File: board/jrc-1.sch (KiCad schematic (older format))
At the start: 0 parts

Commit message: WIP
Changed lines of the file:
@@
 $Descr USLetter 11000 8500
 encoding utf-8
-Sheet 1 2
+Sheet 1 8
 Title "JRC-3"
 Date ""
@@
 $EndDescr
 $Sheet
-S 2600 2450 2350 1550
+S 900  900  1150 750
 U 60EE1618
 F0 "Sheet60EE1617" 50
-F1 "core.sch" 50
+F1 "cpu.sch" 50
+$EndSheet
+$Sheet
+S 3400 900  1150 750
+U 61B43476
+F0 "VIA" 50
+F1 "via.sch" 50
+$EndSheet
+$Sheet
+S 4650 900  1150 750
+U 62053498
+F0 "UART" 50
+F1 "uart.sch" 50
+$EndSheet
+$Sheet
+S 2150 1900 1150 750
+U 61ADDFAC
+F0 "Sheet61ADDFAB" 50
+F1 "memory.sch" 50
+$EndSheet
+$Sheet
+S 5900 850  1150 750
+U 626CE278
+F0 "Clock Circuit" 50
+F1 "clock.sch" 50
+$EndSheet
+$Sheet
+S 3900 1900 1700 1250
+U 62BE9D15
+F0 "Ports & Slots" 50
+F1 "ports.sch" 50
+$EndSheet
+$Sheet
+S 2150 900  1150 750
+U 6224E7FB
+F0 "CPLD Logic" 50
+F1 "cpld.sch" 50
 $EndSheet
 $EndSCHEMATC

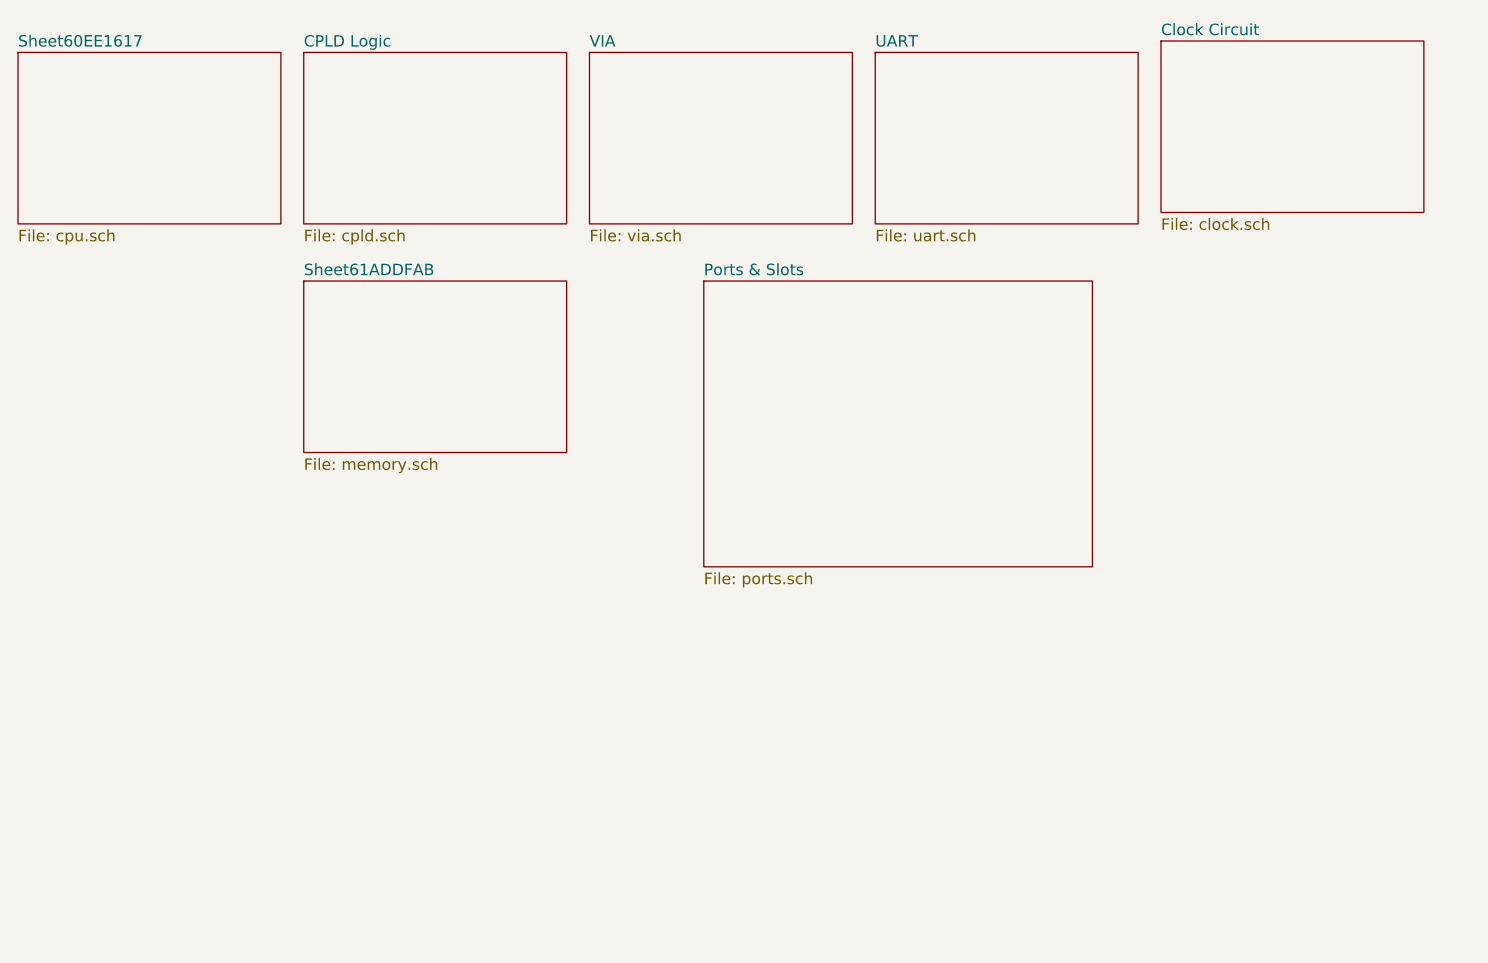
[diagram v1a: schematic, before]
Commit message: RC1 of schematic and initial board layout
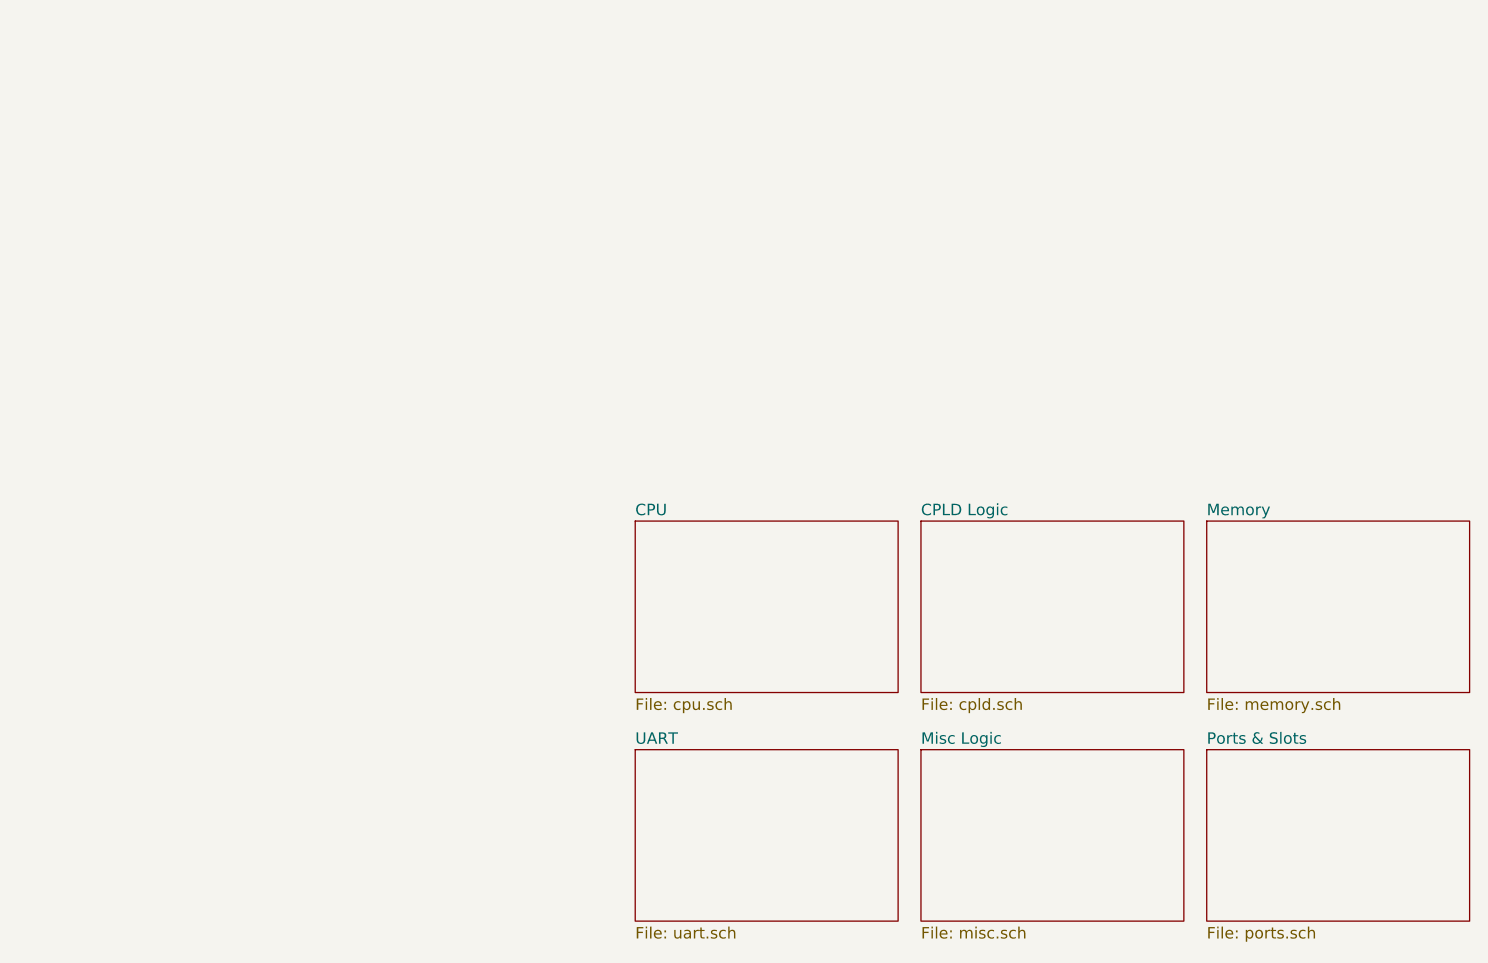
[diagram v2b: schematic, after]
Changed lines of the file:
@@
 $Descr USLetter 11000 8500
 encoding utf-8
-Sheet 1 8
-Title "JRC-3"
-Date ""
-Rev ""
+Sheet 1 7
+Title "JRC-1 Root Sheet"
+Date "2021-12-10"
+Rev "1.0"
 Comp ""
 Comment1 ""
@@
 $EndDescr
 $Sheet
-S 900  900  1150 750
+S 6100 2950 1150 750
+U 61ADDFAC
+F0 "Memory" 50
+F1 "memory.sch" 50
+$EndSheet
+$Sheet
+S 4850 2950 1150 750
+U 6224E7FB
+F0 "CPLD Logic" 50
+F1 "cpld.sch" 50
+$EndSheet
+$Sheet
+S 3600 2950 1150 750
 U 60EE1618
-F0 "Sheet60EE1617" 50
+F0 "CPU" 50
 F1 "cpu.sch" 50
 $EndSheet
 $Sheet
-S 3400 900  1150 750
-U 61B43476
-F0 "VIA" 50
-F1 "via.sch" 50
+S 6100 3950 1150 750
+U 62BE9D15
+F0 "Ports & Slots" 50
+F1 "ports.sch" 50
 $EndSheet
 $Sheet
-S 4650 900  1150 750
+S 3600 3950 1150 750
 U 62053498
 F0 "UART" 50
@@
 $EndSheet
 $Sheet
-S 2150 1900 1150 750
-U 61ADDFAC
-F0 "Sheet61ADDFAB" 50
-F1 "memory.sch" 50
-$EndSheet
-$Sheet
-S 5900 850  1150 750
+S 4850 3950 1150 750
 U 626CE278
-F0 "Clock Circuit" 50
-F1 "clock.sch" 50
-$EndSheet
-$Sheet
-S 3900 1900 1700 1250
-U 62BE9D15
-F0 "Ports & Slots" 50
-F1 "ports.sch" 50
-$EndSheet
-$Sheet
-S 2150 900  1150 750
-U 6224E7FB
-F0 "CPLD Logic" 50
-F1 "cpld.sch" 50
+F0 "Misc Logic" 50
+F1 "misc.sch" 50
 $EndSheet
 $EndSCHEMATC
